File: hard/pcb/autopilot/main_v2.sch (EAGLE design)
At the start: 168 parts, among them IC1 24AA32ASN, IC2 INA194, IC3 LP2950Z, Q1 IRLML5203, Q3 IRLML5203, Q4 IRLML5203, T3 BC848, U2 TMP75DGK, U44 BMP085, X1 USB-SMD-NS

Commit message: nop
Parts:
- removed R26, R37: 0, SparkFun:RESISTOR0805-RES
- added VD5: BAR43, barthess:BAR43
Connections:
- removed net N$31: DD1.PB14, R26.2, R37.2
- removed net XBEE_RTS: JP1.6, R37.1
- net 3.3V: now also VD5.A
- net N$33: now also VD5.C
- net SPI2_MISO_UEXT: now also DD1.PB14; no longer R26.1
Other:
- note added: "xbee_RTS"
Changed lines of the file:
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@@
 <part name="P+20" library="SparkFun" deviceset="3.3V" device=""/>
 <part name="R25" library="SparkFun" deviceset="RESISTOR" device="0805-RES" value="2.7k"/>
-<part name="R26" library="SparkFun" deviceset="RESISTOR" device="0805-RES" value="0"/>
-<part name="R37" library="SparkFun" deviceset="RESISTOR" device="0805-RES" value="0"/>
 <part name="R38" library="SparkFun" deviceset="RESISTOR" device="0805-RES" value="330"/>
 <part name="R39" library="SparkFun" deviceset="RESISTOR" device="0805-RES" value="330"/>
@@
 <part name="F1" library="barthess" deviceset="POLYSWITCH" device=""/>
 <part name="C46" library="SparkFun" deviceset="CAP" device="0805" value="0.1uF"/>
+<part name="VD5" library="barthess" deviceset="BAR43" device=""/>
+<part name="P+21" library="SparkFun" deviceset="3.3V" device=""/>
 </parts>
 <sheets>
@@
 <text x="177.8" y="131.572" size="1.27" layer="98">xbee_sleep</text>
 <text x="41.91" y="-51.308" size="1.27" layer="98">an_reserved</text>
+<text x="208.28" y="136.652" size="1.27" layer="98">xbee_RTS</text>
 </plain>
 <instances>
@@
 <instance part="P+20" gate="G$1" x="63.5" y="86.36"/>
 <instance part="R25" gate="G$1" x="63.5" y="76.2" rot="R90"/>
-<instance part="R26" gate="G$1" x="76.2" y="50.8" rot="MR0"/>
-<instance part="R37" gate="G$1" x="76.2" y="45.72" rot="MR0"/>
 <instance part="R38" gate="G$1" x="-101.6" y="-175.26" rot="R90"/>
 <instance part="R39" gate="G$1" x="-88.9" y="-175.26" rot="R90"/>
@@
 <instance part="F1" gate="G$1" x="-304.8" y="5.08"/>
 <instance part="C46" gate="G$1" x="-43.18" y="58.42"/>
+<instance part="VD5" gate="1" x="-63.5" y="76.2" rot="R270"/>
+<instance part="P+21" gate="G$1" x="-63.5" y="81.28"/>
 </instances>
 <busses>
@@
 <pinref part="P+22" gate="G$1" pin="3.3V"/>
 <wire x1="190.5" y1="200.66" x2="185.42" y2="200.66" width="0.1524" layer="91"/>
+</segment>
+<segment>
+<pinref part="P+21" gate="G$1" pin="3.3V"/>
+<pinref part="VD5" gate="1" pin="A"/>
+<wire x1="-63.5" y1="81.28" x2="-63.5" y2="78.74" width="0.1524" layer="91"/>
 </segment>
 </net>
@@
 </segment>
 </net>
-<net name="XBEE_RTS" class="0">
-<segment>
-<wire x1="205.74" y1="137.16" x2="213.36" y2="137.16" width="0.1524" layer="91"/>
-<label x="213.36" y="137.16" size="1.27" layer="95" xref="yes"/>
-<pinref part="JP1" gate="G$1" pin="6"/>
-</segment>
-<segment>
-<pinref part="R37" gate="G$1" pin="1"/>
-<wire x1="81.28" y1="45.72" x2="83.82" y2="45.72" width="0.1524" layer="91"/>
-<label x="83.82" y="45.72" size="1.27" layer="95" xref="yes"/>
-</segment>
-</net>
 <net name="TO_GPS" class="0">
 <segment>
@@
 </segment>
 </net>
-<net name="N$31" class="0">
-<segment>
-<pinref part="DD1" gate="G$1" pin="PB14"/>
-<wire x1="40.64" y1="48.26" x2="68.58" y2="48.26" width="0.1524" layer="91"/>
-<pinref part="R26" gate="G$1" pin="2"/>
-<wire x1="71.12" y1="50.8" x2="68.58" y2="50.8" width="0.1524" layer="91"/>
-<wire x1="68.58" y1="50.8" x2="68.58" y2="48.26" width="0.1524" layer="91"/>
-<pinref part="R37" gate="G$1" pin="2"/>
-<wire x1="71.12" y1="45.72" x2="68.58" y2="45.72" width="0.1524" layer="91"/>
-<wire x1="68.58" y1="45.72" x2="68.58" y2="48.26" width="0.1524" layer="91"/>
-<junction x="68.58" y="48.26"/>
-</segment>
-</net>
 <net name="SPI2_MOSI_UEXT" class="0">
 <segment>
@@
 <net name="SPI2_MISO_UEXT" class="0">
 <segment>
-<pinref part="R26" gate="G$1" pin="1"/>
-<wire x1="81.28" y1="50.8" x2="83.82" y2="50.8" width="0.1524" layer="91"/>
-<label x="83.82" y="50.8" size="1.27" layer="95" xref="yes"/>
+<label x="48.26" y="48.26" size="1.27" layer="95" xref="yes"/>
+<pinref part="DD1" gate="G$1" pin="PB14"/>
+<wire x1="40.64" y1="48.26" x2="48.26" y2="48.26" width="0.1524" layer="91"/>
 </segment>
 <segment>
@@
 <wire x1="-63.5" y1="68.58" x2="-76.2" y2="68.58" width="0.1524" layer="91"/>
 <junction x="-63.5" y="68.58"/>
-</segment>
-</net>
+<pinref part="VD5" gate="1" pin="C"/>
+<wire x1="-63.5" y1="68.58" x2="-63.5" y2="73.66" width="0.1524" layer="91"/>
+</segment>
+</net>

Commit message: nop
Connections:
- removed net TMP75_ALERT: DD1.PE6, U2.ALERT
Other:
- note added: "TMP75_alert"
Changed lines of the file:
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@@
 <text x="41.91" y="-51.308" size="1.27" layer="98">an_reserved</text>
 <text x="208.28" y="136.652" size="1.27" layer="98">xbee_RTS</text>
+<text x="284.48" y="-15.748" size="1.27" layer="98">TMP75_alert</text>
 </plain>
 <instances>
@@
 </segment>
 </net>
-<net name="TMP75_ALERT" class="0">
-<segment>
-<wire x1="297.18" y1="-15.24" x2="294.64" y2="-15.24" width="0.1524" layer="91"/>
-<label x="294.64" y="-15.24" size="1.27" layer="95" rot="R180" xref="yes"/>
-<pinref part="U2" gate="G$1" pin="ALERT"/>
-</segment>
-<segment>
-<label x="48.26" y="-10.16" size="1.27" layer="95" xref="yes"/>
-<pinref part="DD1" gate="G$1" pin="PE6"/>
-<wire x1="48.26" y1="-10.16" x2="40.64" y2="-10.16" width="0.1524" layer="91"/>
-</segment>
-</net>

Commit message: nop
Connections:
- net 5V_ENABLE: now also DD1.PD10; no longer DD1.PA8
- net ADIS_NRST: now also DD1.PA8; no longer DD1.PD10
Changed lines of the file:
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@@
 </segment>
 </net>
-<net name="+3.3V_A" class="2">
+<net name="+3.3V_A" class="0">
 <segment>
 <wire x1="345.44" y1="-109.22" x2="345.44" y2="-119.38" width="0.1524" layer="91"/>
@@
 <net name="5V_ENABLE" class="0">
 <segment>
-<label x="48.26" y="20.32" size="1.27" layer="95" xref="yes"/>
-<wire x1="40.64" y1="20.32" x2="48.26" y2="20.32" width="0.1524" layer="91"/>
-<pinref part="DD1" gate="G$1" pin="PA8"/>
-</segment>
-<segment>
 <wire x1="-317.5" y1="-96.52" x2="-320.04" y2="-96.52" width="0.1524" layer="91"/>
 <label x="-320.04" y="-96.52" size="1.27" layer="95" rot="R180" xref="yes"/>
 <pinref part="R61" gate="G$1" pin="2"/>
+</segment>
+<segment>
+<wire x1="-38.1" y1="-63.5" x2="-33.02" y2="-63.5" width="0.1524" layer="91"/>
+<label x="-38.1" y="-63.5" size="1.27" layer="95" rot="R180" xref="yes"/>
+<pinref part="DD1" gate="G$1" pin="PD10"/>
 </segment>
 </net>
@@
 </segment>
 </net>
-<net name="GND_A" class="3">
+<net name="GND_A" class="0">
 <segment>
 <label x="-48.26" y="55.88" size="1.27" layer="95" rot="R180" xref="yes"/>
@@
 </segment>
 <segment>
-<wire x1="-38.1" y1="-63.5" x2="-33.02" y2="-63.5" width="0.1524" layer="91"/>
-<label x="-38.1" y="-63.5" size="1.27" layer="95" rot="R180" xref="yes"/>
-<pinref part="DD1" gate="G$1" pin="PD10"/>
-</segment>
-</net>
+<label x="48.26" y="20.32" size="1.27" layer="95" xref="yes"/>
+<wire x1="40.64" y1="20.32" x2="48.26" y2="20.32" width="0.1524" layer="91"/>
+<pinref part="DD1" gate="G$1" pin="PA8"/>
+</segment>
+</net>

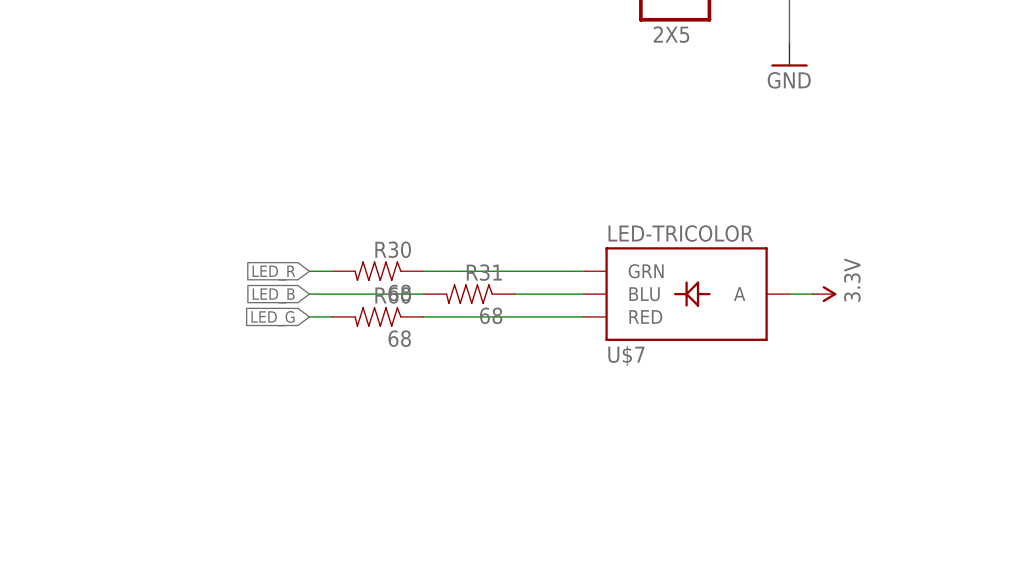
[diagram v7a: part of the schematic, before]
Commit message: Added 5mm 3color led
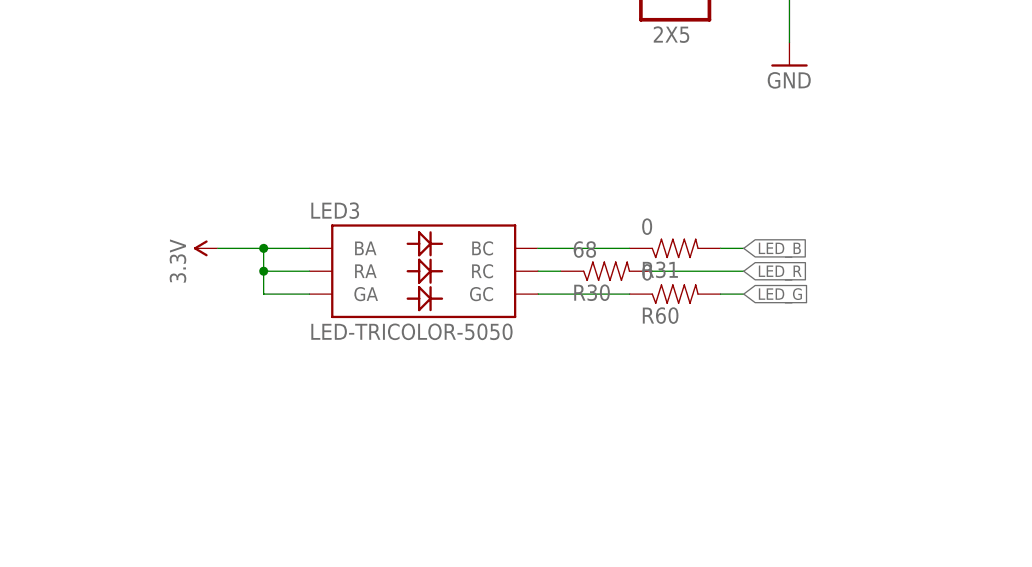
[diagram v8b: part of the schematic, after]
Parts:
- removed U$7: LED-TRICOLOR, SparkFun:LED-TRICOLOR
- added LED3: LED-TRICOLOR-5050, barthess:LED-TRICOLOR-5050
- R31, R60: value 68 -> 0
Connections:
- removed net N$56: R31.1, U$7.BLU
- new net N$31: LED3.GC, R60.1
- net 3.3V: now also LED3.BA, LED3.GA, LED3.RA; no longer U$7.A
- net N$12: now also LED3.RC, R30.1; no longer R60.1, U$7.RED
- net N$8: now also LED3.BC, R31.1; no longer R30.1, U$7.GRN
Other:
- moved on the sheet: R30, R31, R60
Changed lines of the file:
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@@
 <part name="C55" library="SparkFun" deviceset="CAP" device="0805" value="0.1uF"/>
 <part name="IC3" library="linear" deviceset="LP2950" device="Z"/>
-<part name="U$7" library="SparkFun" deviceset="LED-TRICOLOR" device=""/>
 <part name="P+23" library="SparkFun" deviceset="3.3V" device=""/>
 <part name="R30" library="SparkFun" deviceset="RESISTOR" device="0805-RES" value="68"/>
-<part name="R31" library="SparkFun" deviceset="RESISTOR" device="0805-RES" value="68"/>
-<part name="R60" library="SparkFun" deviceset="RESISTOR" device="0805-RES" value="68"/>
+<part name="R31" library="SparkFun" deviceset="RESISTOR" device="0805-RES" value="0"/>
+<part name="R60" library="SparkFun" deviceset="RESISTOR" device="0805-RES" value="0"/>
 <part name="T3" library="transistor" deviceset="BC848" device=""/>
 <part name="R61" library="SparkFun" deviceset="RESISTOR" device="0805-RES" value="1k"/>
@@
 <part name="VD5" library="barthess" deviceset="BAR43" device=""/>
 <part name="P+21" library="SparkFun" deviceset="3.3V" device=""/>
+<part name="LED3" library="barthess" deviceset="LED-TRICOLOR-5050" device=""/>
 </parts>
 <sheets>
@@
 <instance part="C55" gate="G$1" x="-266.7" y="-109.22"/>
 <instance part="IC3" gate="G$1" x="-243.84" y="-101.6"/>
-<instance part="U$7" gate="G$1" x="198.12" y="96.52" rot="MR180"/>
-<instance part="P+23" gate="G$1" x="213.36" y="99.06" rot="MR90"/>
-<instance part="R30" gate="G$1" x="165.1" y="101.6" rot="MR0"/>
-<instance part="R31" gate="G$1" x="175.26" y="99.06" rot="MR0"/>
-<instance part="R60" gate="G$1" x="165.1" y="96.52" rot="MR0"/>
+<instance part="P+23" gate="G$1" x="147.32" y="104.14" rot="MR270"/>
+<instance part="R30" gate="G$1" x="190.5" y="101.6" rot="MR180"/>
+<instance part="R31" gate="G$1" x="198.12" y="104.14" rot="MR180"/>
+<instance part="R60" gate="G$1" x="198.12" y="99.06" rot="MR180"/>
 <instance part="T3" gate="G$1" x="-302.26" y="-96.52"/>
 <instance part="R61" gate="G$1" x="-312.42" y="-96.52" rot="R180"/>
@@
 <instance part="VD5" gate="1" x="-63.5" y="76.2" rot="R270"/>
 <instance part="P+21" gate="G$1" x="-63.5" y="81.28"/>
+<instance part="LED3" gate="G$1" x="170.18" y="101.6"/>
 </instances>
 <busses>
@@
 </segment>
 <segment>
-<wire x1="213.36" y1="99.06" x2="210.82" y2="99.06" width="0.1524" layer="91"/>
 <pinref part="P+23" gate="G$1" pin="3.3V"/>
-<pinref part="U$7" gate="G$1" pin="A"/>
+<pinref part="LED3" gate="G$1" pin="BA"/>
+<wire x1="147.32" y1="104.14" x2="152.4" y2="104.14" width="0.1524" layer="91"/>
+<pinref part="LED3" gate="G$1" pin="RA"/>
+<wire x1="152.4" y1="104.14" x2="157.48" y2="104.14" width="0.1524" layer="91"/>
+<wire x1="157.48" y1="101.6" x2="152.4" y2="101.6" width="0.1524" layer="91"/>
+<wire x1="152.4" y1="101.6" x2="152.4" y2="104.14" width="0.1524" layer="91"/>
+<junction x="152.4" y="104.14"/>
+<pinref part="LED3" gate="G$1" pin="GA"/>
+<wire x1="157.48" y1="99.06" x2="152.4" y2="99.06" width="0.1524" layer="91"/>
+<wire x1="152.4" y1="99.06" x2="152.4" y2="101.6" width="0.1524" layer="91"/>
+<junction x="152.4" y="101.6"/>
 </segment>
 <segment>
@@
 </segment>
 </net>
-<net name="N$56" class="0">
-<segment>
-<wire x1="187.96" y1="99.06" x2="180.34" y2="99.06" width="0.1524" layer="91"/>
-<pinref part="U$7" gate="G$1" pin="BLU"/>
-<pinref part="R31" gate="G$1" pin="1"/>
-</segment>
-</net>
 <net name="LED_G" class="0">
 <segment>
-<wire x1="160.02" y1="96.52" x2="157.48" y2="96.52" width="0.1524" layer="91"/>
-<label x="157.48" y="96.52" size="1.27" layer="95" rot="MR0" xref="yes"/>
+<wire x1="203.2" y1="99.06" x2="205.74" y2="99.06" width="0.1524" layer="91"/>
+<label x="205.74" y="99.06" size="1.27" layer="95" rot="MR180" xref="yes"/>
 <pinref part="R60" gate="G$1" pin="2"/>
 </segment>
@@
 <net name="LED_B" class="0">
 <segment>
-<wire x1="170.18" y1="99.06" x2="157.48" y2="99.06" width="0.1524" layer="91"/>
-<label x="157.48" y="99.06" size="1.27" layer="95" rot="MR0" xref="yes"/>
+<wire x1="203.2" y1="104.14" x2="205.74" y2="104.14" width="0.1524" layer="91"/>
+<label x="205.74" y="104.14" size="1.27" layer="95" rot="MR180" xref="yes"/>
 <pinref part="R31" gate="G$1" pin="2"/>
 </segment>
@@
 <net name="LED_R" class="0">
 <segment>
-<wire x1="160.02" y1="101.6" x2="157.48" y2="101.6" width="0.1524" layer="91"/>
-<label x="157.48" y="101.6" size="1.27" layer="95" rot="MR0" xref="yes"/>
+<wire x1="195.58" y1="101.6" x2="205.74" y2="101.6" width="0.1524" layer="91"/>
+<label x="205.74" y="101.6" size="1.27" layer="95" rot="MR180" xref="yes"/>
 <pinref part="R30" gate="G$1" pin="2"/>
 </segment>
@@
 </segment>
 </net>
-<net name="N$8" class="0">
-<segment>
-<pinref part="R30" gate="G$1" pin="1"/>
-<pinref part="U$7" gate="G$1" pin="GRN"/>
-<wire x1="170.18" y1="101.6" x2="187.96" y2="101.6" width="0.1524" layer="91"/>
-</segment>
-</net>
-<net name="N$12" class="0">
-<segment>
-<pinref part="R60" gate="G$1" pin="1"/>
-<pinref part="U$7" gate="G$1" pin="RED"/>
-<wire x1="170.18" y1="96.52" x2="187.96" y2="96.52" width="0.1524" layer="91"/>
-</segment>
-</net>
 <net name="N$33" class="0">
 <segment>
@@
 </segment>
 </net>
+<net name="N$8" class="0">
+<segment>
+<pinref part="R31" gate="G$1" pin="1"/>
+<pinref part="LED3" gate="G$1" pin="BC"/>
+<wire x1="193.04" y1="104.14" x2="182.88" y2="104.14" width="0.1524" layer="91"/>
+</segment>
+</net>
+<net name="N$12" class="0">
+<segment>
+<pinref part="R30" gate="G$1" pin="1"/>
+<pinref part="LED3" gate="G$1" pin="RC"/>
+<wire x1="185.42" y1="101.6" x2="182.88" y2="101.6" width="0.1524" layer="91"/>
+</segment>
+</net>
+<net name="N$31" class="0">
+<segment>
+<pinref part="R60" gate="G$1" pin="1"/>
+<pinref part="LED3" gate="G$1" pin="GC"/>
+<wire x1="193.04" y1="99.06" x2="182.88" y2="99.06" width="0.1524" layer="91"/>
+</segment>
+</net>
